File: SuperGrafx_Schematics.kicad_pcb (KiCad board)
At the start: 2 copper layers, 5 parts, among them IC105 HuC6202, IC110 HSRM20256LM, J1 PC_Engine_Hucard_slot, J3 Mini-DIN-8

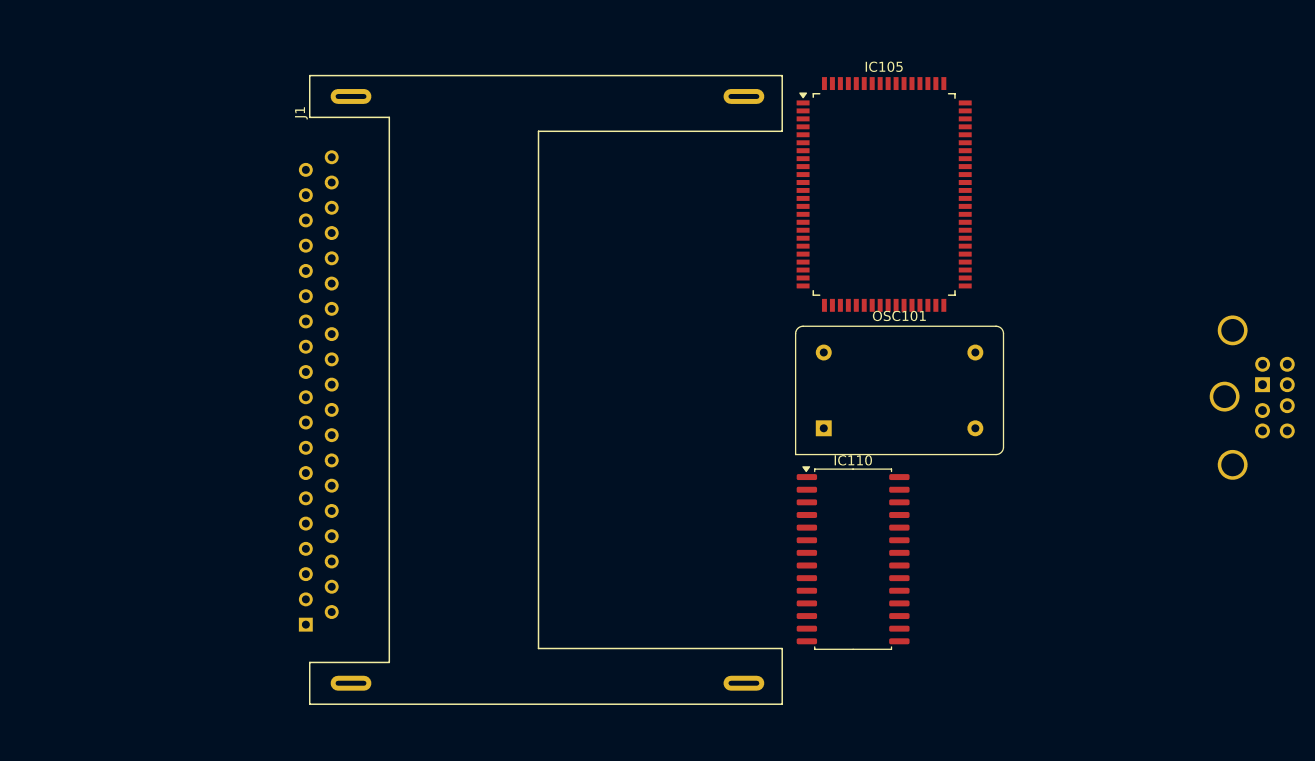
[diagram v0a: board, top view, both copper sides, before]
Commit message: Missed out CD dection signal to main CPU and found values of decoupling capacitors under CPU hidden by EMI shield.
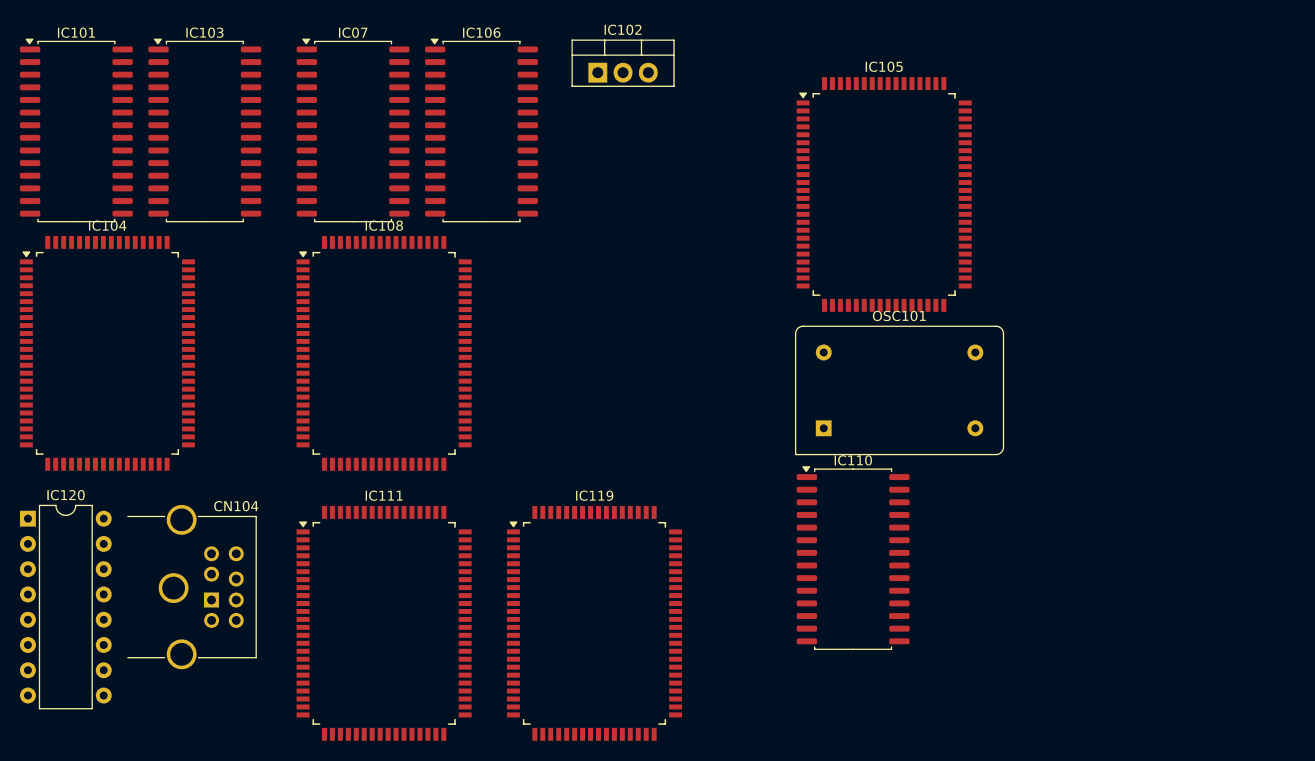
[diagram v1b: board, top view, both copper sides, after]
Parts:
- removed J1: PC_Engine_Hucard_slot, SNES:PC-Engine_slot
- removed J3: Mini-DIN-8, SNES:1658998-1
- added CN104: Mini-DIN-8, SNES:1658998-1, F.Cu at (65.7, 109.3)
- added IC07: HSRM20256LM, Package_SO:SOIC-28W_7.5x17.9mm_P1.27mm, F.Cu at (88.5, 63.5)
- added IC101: HSRM20256LM, Package_SO:SOIC-28W_7.5x17.9mm_P1.27mm, F.Cu at (60.7, 63.5)
- added IC102: LM7805_TO220, Package_TO_SOT_THT:TO-220-3_Vertical, F.Cu at (113.1, 57.6)
- added IC103: HSRM20256LM, Package_SO:SOIC-28W_7.5x17.9mm_P1.27mm, F.Cu at (73.6, 63.5)
- added IC104: HuC6270, Package_QFP:PQFP-80_14x20mm_P0.8mm, F.Cu at (63.8, 85.8)
- added IC106: HSRM20256LM, Package_SO:SOIC-28W_7.5x17.9mm_P1.27mm, F.Cu at (101.4, 63.5)
- added IC108: HuC6270, Package_QFP:PQFP-80_14x20mm_P0.8mm, F.Cu at (91.6, 85.8)
- added IC111: HuC6280, Package_QFP:PQFP-80_14x20mm_P0.8mm, F.Cu at (91.6, 113.0)
- added IC119: HuC6260, Package_QFP:PQFP-80_14x20mm_P0.8mm, F.Cu at (112.8, 113.0)
- added IC120: MC74HC157N, Package_DIP:CERDIP-16_W7.62mm_SideBrazed, F.Cu at (55.8, 102.5)
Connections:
- IC105 pad 25: /A2 -> /VPC_A2
- IC105 pad 26: /A1 -> /VPC_A1
- IC105 pad 27: /A0 -> /VPC_A0
- IC105 pad 28: Net-(IC105-DOTCK) -> /HSYNC
- IC105 pad 30: Net-(IC105-~{HSYNC}) -> /DOTCK
- IC105 pad 32: /VD8 -> /VCE, VIDEO & AUDIO AMPLIFICATION/VD8
- IC105 pad 33: /VD7 -> /VCE, VIDEO & AUDIO AMPLIFICATION/VD7
- IC105 pad 34: /VD6 -> /VCE, VIDEO & AUDIO AMPLIFICATION/VD6
- IC105 pad 35: /VD5 -> /VCE, VIDEO & AUDIO AMPLIFICATION/VD5
- IC105 pad 36: /VD4 -> /VCE, VIDEO & AUDIO AMPLIFICATION/VD4
- IC105 pad 37: /VD3 -> /VCE, VIDEO & AUDIO AMPLIFICATION/VD3
- IC105 pad 38: /VD2 -> /VCE, VIDEO & AUDIO AMPLIFICATION/VD2
- IC105 pad 39: /VD1 -> /VCE, VIDEO & AUDIO AMPLIFICATION/VD1
- IC105 pad 40: /VD0 -> /VCE, VIDEO & AUDIO AMPLIFICATION/VD0
- IC105 pad 46: unconnected-(IC105-V1D0-Pad46) -> /VDC1/V1D0
- IC105 pad 47: unconnected-(IC105-V1D1-Pad47) -> /VDC1/V1D1
- IC105 pad 48: unconnected-(IC105-V1D2-Pad48) -> /VDC1/V1D2
- IC105 pad 49: unconnected-(IC105-V1D3-Pad49) -> /VDC1/V1D3
- IC105 pad 50: unconnected-(IC105-V1D4-Pad50) -> /VDC1/V1D4
- IC105 pad 51: unconnected-(IC105-V1D5-Pad51) -> /VDC1/V1D5
- IC105 pad 52: unconnected-(IC105-V1D6-Pad52) -> /VDC1/V1D6
- IC105 pad 53: unconnected-(IC105-V1D7-Pad53) -> /VDC1/V1D7
- IC105 pad 54: unconnected-(IC105-V1D8-Pad54) -> /VDC1/V1D8
- IC105 pad 55: unconnected-(IC105-~{VDC1_CS}-Pad55) -> /~{VDC1_CS}
- IC105 pad 56: unconnected-(IC105-~{VDC2_CS}-Pad56) -> /~{VDC2_CS}
- IC105 pad 57: unconnected-(IC105-V2D0-Pad57) -> /VDC2/V2D0
- IC105 pad 58: unconnected-(IC105-V2D1-Pad58) -> /VDC2/V2D1
- IC105 pad 59: unconnected-(IC105-V2D2-Pad59) -> /VDC2/V2D2
- IC105 pad 60: unconnected-(IC105-V2D3-Pad60) -> /VDC2/V2D3
- IC105 pad 61: unconnected-(IC105-V2D4-Pad61) -> /VDC2/V2D4
- IC105 pad 65: unconnected-(IC105-V2D5-Pad65) -> /VDC2/V2D5
- IC105 pad 66: unconnected-(IC105-V2D6-Pad66) -> /VDC2/V2D6
- IC105 pad 67: unconnected-(IC105-V2D7-Pad67) -> /VDC2/V2D7
- IC105 pad 68: unconnected-(IC105-V2D8-Pad68) -> /VDC2/V2D8
- IC105 pad 71: /D0 -> /VPC_D0
- IC105 pad 72: /D1 -> /VPC_D1
- IC105 pad 73: /D2 -> /VPC_D2
- IC105 pad 74: /D3 -> /VPC_D3
- IC105 pad 75: /D4 -> /VPC_D4
- IC105 pad 76: /D5 -> /VPC_D5
- IC105 pad 77: /D6 -> /VPC_D6
- IC105 pad 78: /D7 -> /VPC_D7
- IC110 pad 20: Net-(IC110-~{CS}) -> /~{RAM_CS}
